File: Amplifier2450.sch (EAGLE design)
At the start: 25 parts, among them IC1 7805DT, Q1 P-KANAL_MOSFET_, X1 SMA-142-0701-801/806, X2 SMA-142-0701-801/806

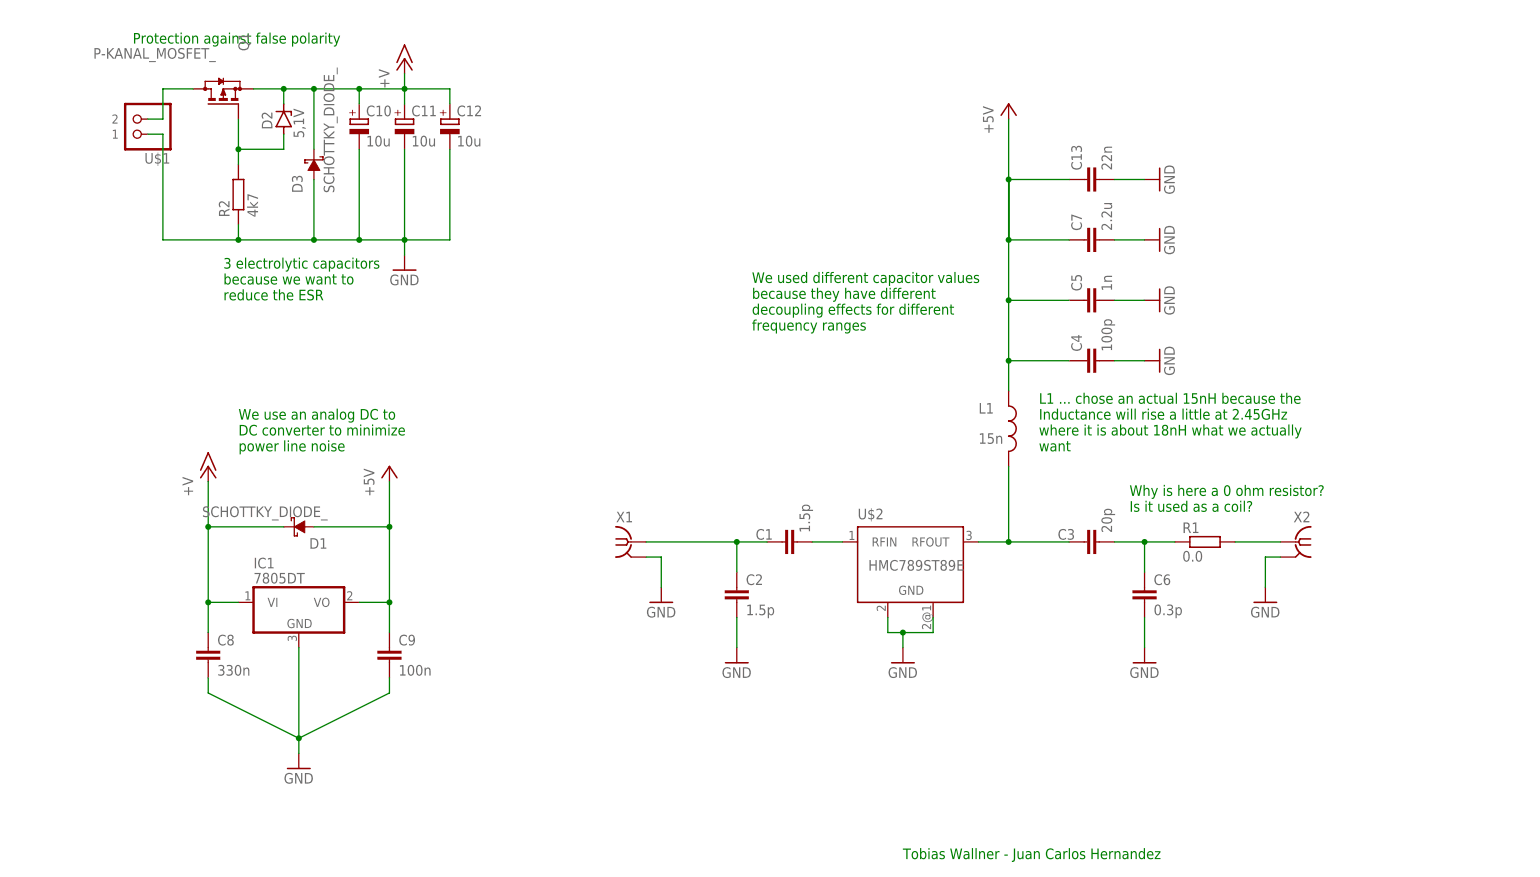
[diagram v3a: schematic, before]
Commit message: (Tobias): halfway applied Roberts feedback
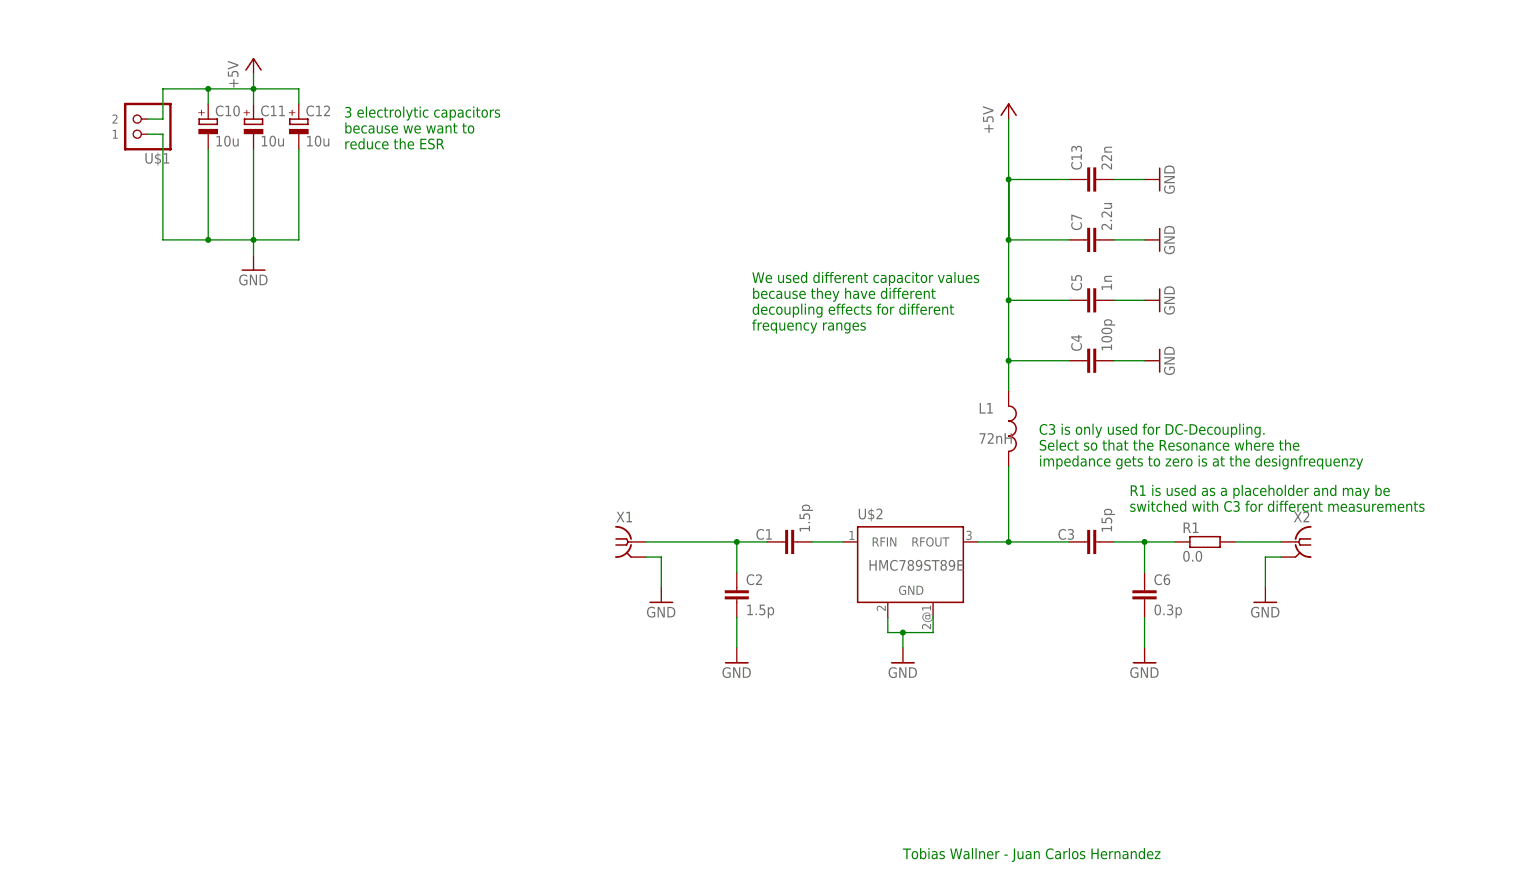
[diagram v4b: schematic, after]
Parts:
- removed C8: 330n, rcl:C-EUC0603
- removed C9: 100n, rcl:C-EUC0603
- removed D1, D3: SCHOTTKY_DIODE_, own_htl3r-discrete-1:SCHOTTKY_DIODE_
- removed D2: 5,1V, diode:ZENER-DIODESOT23
- removed IC1: 7805DT, linear:7824DT
- removed Q1: P-KANAL_MOSFET_, own_htl3r-discrete-1:P-KANAL_MOSFET_
- removed R2: 4k7, rcl:R-EU_R0805
- C3: value 20p -> 15p
- L1: value 15n -> 72nH
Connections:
- removed net +15V: C10.+, C11.+, C12.+, C8.1, D1.C, D2.C, D3.C, IC1.VI, Q1.S
- removed net N$6: Q1.D, U$1.2
- removed net N$7: D2.A, Q1.G, R2.2
- net +5V: now also C10.+, C11.+, C12.+, U$1.2; no longer C9.1, D1.A, IC1.VO
- net GND: no longer C8.2, C9.2, D3.A, IC1.GND, R2.1
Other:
- note added: "C3 is only used for DC-Decoupling. Select so that the Resonance where the impedance gets to zero is at the designfrequenzy"
- note added: "R1 is used as a placeholder and may be switched with C3 for different measurements"
- note removed: "L1 ... chose an actual 15nH because the Inductance will rise a little at 2.45GHz where it is about 18nH what we actually want"
- note removed: "Protection against false polarity"
- note removed: "We use an analog DC to DC converter to minimize power line noise"
- note removed: "Why is here a 0 ohm resistor? Is it used as a coil?"
- moved on the sheet: C10, C11, C12

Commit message: (Tobias): added documentation to the current design, explaining why certain parts and decisions have been made
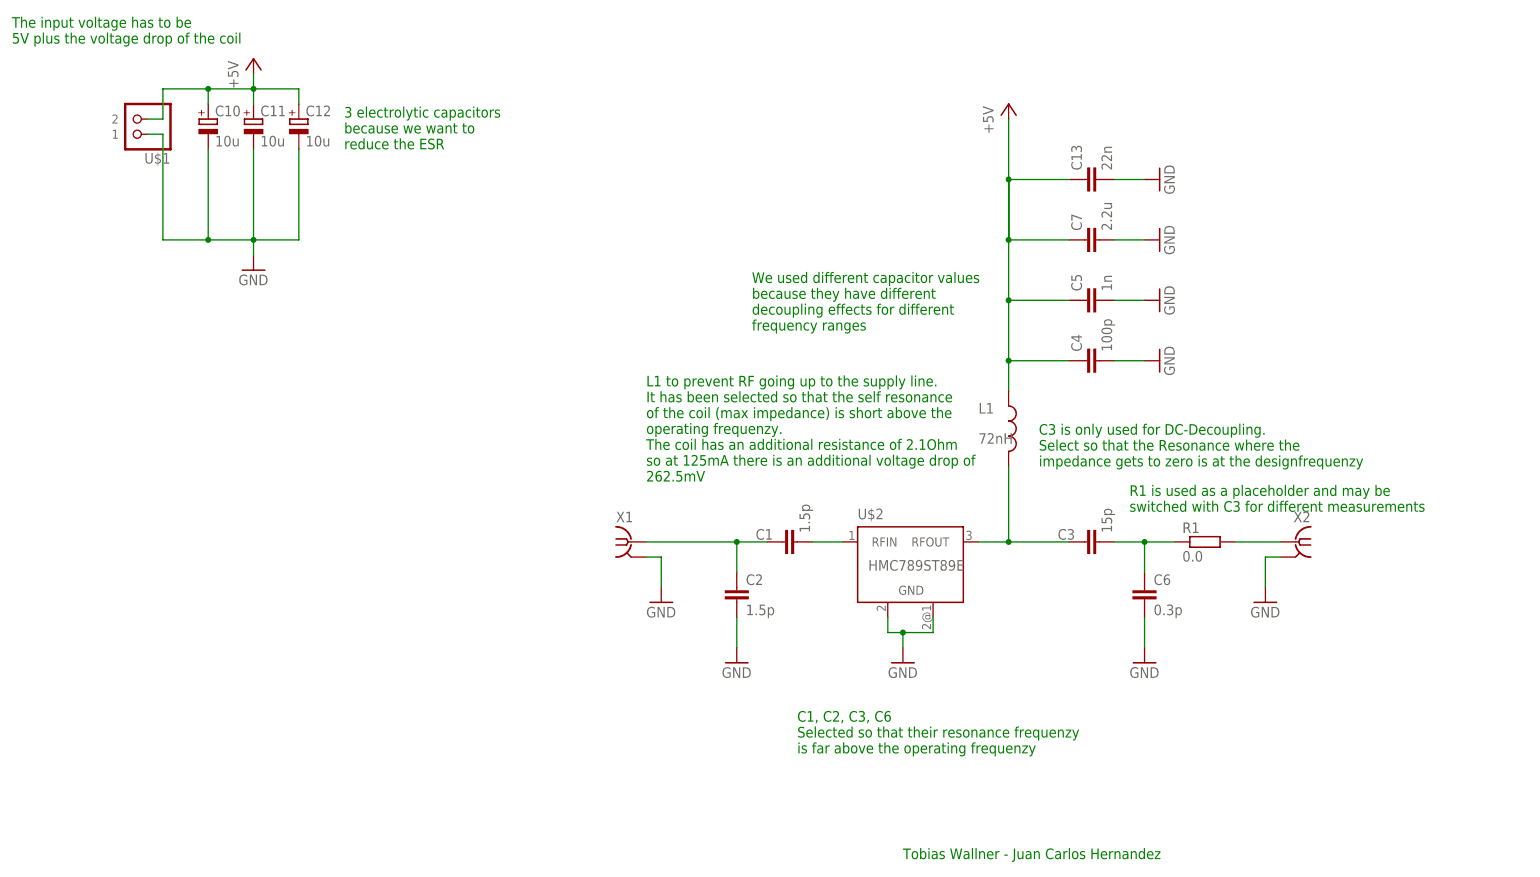
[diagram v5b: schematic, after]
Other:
- note added: "C1, C2, C3, C6 Selected so that their resonance frequenzy is far above the operating frequenzy"
- note added: "L1 to prevent RF going up to the supply line. It has been selected so that the self resonance of the coil (max impedance) is short above the operating frequenzy. The coil has an additional resistance of 2.1Ohm so at 125mA there is an additional voltage drop of 262.5mV"
- note added: "The input voltage has to be 5V plus the voltage drop of the coil"
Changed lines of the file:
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@@
 Select so that the Resonance where the
 impedance gets to zero is at the designfrequenzy</text>
+<text x="147.32" y="30.48" size="1.778" layer="91">C1, C2, C3, C6
+Selected so that their resonance frequenzy
+is far above the operating frequenzy</text>
+<text x="121.92" y="76.2" size="1.778" layer="91">L1 to prevent RF going up to the supply line.
+It has been selected so that the self resonance
+of the coil (max impedance) is short above the
+operating frequenzy.
+The coil has an additional resistance of 2.1Ohm
+so at 125mA there is an additional voltage drop of
+262.5mV</text>
+<text x="15.24" y="149.86" size="1.778" layer="91">The input voltage has to be
+5V plus the voltage drop of the coil</text>
 </plain>
 <instances>

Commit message: (Tobias): made finishing touches to the design
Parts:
- removed C10, C11, C12: 10u, rcl:CPOL-EUE2.5-5
- C1, C2, C3, C6: device rcl:C-EUC0402 -> rcl:C-EUC0603
- L1: device own_htl3r-discrete-1:L_US_ -> rcl:C-EUC0603
- R1: device rcl:R-EU_R0402 -> rcl:C-EUC0603
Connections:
- net +5V: no longer C10.+, C11.+, C12.+
- net GND: no longer C10.-, C11.-, C12.-
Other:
- note removed: "3 electrolytic capacitors because we want to reduce the ESR"
- moved on the sheet: C13, C7, R1, U$1
